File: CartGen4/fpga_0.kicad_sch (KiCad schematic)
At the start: 12 parts, among them U9 LFXP2-8E-5MN132C

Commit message: Assigned all footprints
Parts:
- C19, C20, C21, C22, C23, C24, C25, C30, C31, C32: footprint Capacitor_SMD:C_0402_1005Metric_Pad0.74x0.62mm_HandSolder -> Capacitor_SMD:C_0603_1608Metric_Pad1.08x0.95mm_HandSolder
- R15: footprint (none) -> Resistor_SMD:R_0603_1608Metric_Pad0.98x0.95mm_HandSolder
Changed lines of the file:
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@@
       (effects (font (size 1.27 1.27)) (justify left))
     )
-    (property "Footprint" "Capacitor_SMD:C_0402_1005Metric_Pad0.74x0.62mm_HandSolder" (id 2) (at 205.4352 33.02 0)
+    (property "Footprint" "Capacitor_SMD:C_0603_1608Metric_Pad1.08x0.95mm_HandSolder" (id 2) (at 205.4352 33.02 0)
       (effects (font (size 1.27 1.27)) hide)
     )
@@
       (effects (font (size 1.27 1.27)) (justify left))
     )
-    (property "Footprint" "Capacitor_SMD:C_0402_1005Metric_Pad0.74x0.62mm_HandSolder" (id 2) (at 40.3352 160.02 0)
+    (property "Footprint" "Capacitor_SMD:C_0603_1608Metric_Pad1.08x0.95mm_HandSolder" (id 2) (at 40.3352 160.02 0)
       (effects (font (size 1.27 1.27)) hide)
     )
@@
       (effects (font (size 1.27 1.27)) (justify left))
     )
-    (property "Footprint" "Capacitor_SMD:C_0402_1005Metric_Pad0.74x0.62mm_HandSolder" (id 2) (at 117.8052 40.64 0)
+    (property "Footprint" "Capacitor_SMD:C_0603_1608Metric_Pad1.08x0.95mm_HandSolder" (id 2) (at 117.8052 40.64 0)
       (effects (font (size 1.27 1.27)) hide)
     )
@@
       (effects (font (size 1.27 1.27)) (justify left))
     )
-    (property "Footprint" "" (id 2) (at 75.692 133.35 90)
+    (property "Footprint" "Resistor_SMD:R_0603_1608Metric_Pad0.98x0.95mm_HandSolder" (id 2) (at 75.692 133.35 90)
       (effects (font (size 1.27 1.27)) hide)
     )
@@
       (effects (font (size 1.27 1.27)) (justify left))
     )
-    (property "Footprint" "Capacitor_SMD:C_0402_1005Metric_Pad0.74x0.62mm_HandSolder" (id 2) (at 181.3052 138.43 0)
+    (property "Footprint" "Capacitor_SMD:C_0603_1608Metric_Pad1.08x0.95mm_HandSolder" (id 2) (at 181.3052 138.43 0)
       (effects (font (size 1.27 1.27)) hide)
     )
@@
       (effects (font (size 1.27 1.27)) (justify left))
     )
-    (property "Footprint" "Capacitor_SMD:C_0402_1005Metric_Pad0.74x0.62mm_HandSolder" (id 2) (at 65.7352 137.16 0)
+    (property "Footprint" "Capacitor_SMD:C_0603_1608Metric_Pad1.08x0.95mm_HandSolder" (id 2) (at 65.7352 137.16 0)
       (effects (font (size 1.27 1.27)) hide)
     )
@@
       (effects (font (size 1.27 1.27)) (justify left))
     )
-    (property "Footprint" "Capacitor_SMD:C_0402_1005Metric_Pad0.74x0.62mm_HandSolder" (id 2) (at 53.0352 137.16 0)
+    (property "Footprint" "Capacitor_SMD:C_0603_1608Metric_Pad1.08x0.95mm_HandSolder" (id 2) (at 53.0352 137.16 0)
       (effects (font (size 1.27 1.27)) hide)
     )
@@
       (effects (font (size 1.27 1.27)) (justify left))
     )
-    (property "Footprint" "Capacitor_SMD:C_0402_1005Metric_Pad0.74x0.62mm_HandSolder" (id 2) (at 27.6352 57.15 0)
+    (property "Footprint" "Capacitor_SMD:C_0603_1608Metric_Pad1.08x0.95mm_HandSolder" (id 2) (at 27.6352 57.15 0)
       (effects (font (size 1.27 1.27)) hide)
     )
@@
       (effects (font (size 1.27 1.27)) (justify left))
     )
-    (property "Footprint" "Capacitor_SMD:C_0402_1005Metric_Pad0.74x0.62mm_HandSolder" (id 2) (at 40.3352 137.16 0)
+    (property "Footprint" "Capacitor_SMD:C_0603_1608Metric_Pad1.08x0.95mm_HandSolder" (id 2) (at 40.3352 137.16 0)
       (effects (font (size 1.27 1.27)) hide)
     )
@@
       (effects (font (size 1.27 1.27)) (justify left))
     )
-    (property "Footprint" "Capacitor_SMD:C_0402_1005Metric_Pad0.74x0.62mm_HandSolder" (id 2) (at 53.0352 160.02 0)
+    (property "Footprint" "Capacitor_SMD:C_0603_1608Metric_Pad1.08x0.95mm_HandSolder" (id 2) (at 53.0352 160.02 0)
       (effects (font (size 1.27 1.27)) hide)
     )
@@
       (effects (font (size 1.27 1.27)) (justify left))
     )
-    (property "Footprint" "Capacitor_SMD:C_0402_1005Metric_Pad0.74x0.62mm_HandSolder" (id 2) (at 65.7352 160.02 0)
-      (effects (font (size 1.27 1.27)) hide)
-    )
+    (property "Footprint" "Capacitor_SMD:C_0603_1608Metric_Pad1.08x0.95mm_HandSolder" (id 2) (at 65.7352 160.02 0)
+      (effects (font (size 1.27 1.27)) hide)
+    )

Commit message: Changed most R and C to 0402 size
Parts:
- C19, C20, C21, C22, C23, C24, C25, C30, C31, C32: footprint Capacitor_SMD:C_0603_1608Metric_Pad1.08x0.95mm_HandSolder -> Capacitor_SMD:C_0402_1005Metric_Pad0.74x0.62mm_HandSolder
- R15: footprint Resistor_SMD:R_0603_1608Metric_Pad0.98x0.95mm_HandSolder -> Resistor_SMD:R_0402_1005Metric_Pad0.72x0.64mm_HandSolder
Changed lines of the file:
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@@
       (effects (font (size 1.27 1.27)) (justify left))
     )
-    (property "Footprint" "Capacitor_SMD:C_0603_1608Metric_Pad1.08x0.95mm_HandSolder" (id 2) (at 205.4352 33.02 0)
+    (property "Footprint" "Capacitor_SMD:C_0402_1005Metric_Pad0.74x0.62mm_HandSolder" (id 2) (at 205.4352 33.02 0)
       (effects (font (size 1.27 1.27)) hide)
     )
@@
       (effects (font (size 1.27 1.27)) (justify left))
     )
-    (property "Footprint" "Capacitor_SMD:C_0603_1608Metric_Pad1.08x0.95mm_HandSolder" (id 2) (at 40.3352 160.02 0)
+    (property "Footprint" "Capacitor_SMD:C_0402_1005Metric_Pad0.74x0.62mm_HandSolder" (id 2) (at 40.3352 160.02 0)
       (effects (font (size 1.27 1.27)) hide)
     )
@@
       (effects (font (size 1.27 1.27)) (justify left))
     )
-    (property "Footprint" "Capacitor_SMD:C_0603_1608Metric_Pad1.08x0.95mm_HandSolder" (id 2) (at 117.8052 40.64 0)
+    (property "Footprint" "Capacitor_SMD:C_0402_1005Metric_Pad0.74x0.62mm_HandSolder" (id 2) (at 117.8052 40.64 0)
       (effects (font (size 1.27 1.27)) hide)
     )
@@
       (effects (font (size 1.27 1.27)) (justify left))
     )
-    (property "Footprint" "Resistor_SMD:R_0603_1608Metric_Pad0.98x0.95mm_HandSolder" (id 2) (at 75.692 133.35 90)
+    (property "Footprint" "Resistor_SMD:R_0402_1005Metric_Pad0.72x0.64mm_HandSolder" (id 2) (at 75.692 133.35 90)
       (effects (font (size 1.27 1.27)) hide)
     )
@@
       (effects (font (size 1.27 1.27)) (justify left))
     )
-    (property "Footprint" "Capacitor_SMD:C_0603_1608Metric_Pad1.08x0.95mm_HandSolder" (id 2) (at 181.3052 138.43 0)
+    (property "Footprint" "Capacitor_SMD:C_0402_1005Metric_Pad0.74x0.62mm_HandSolder" (id 2) (at 181.3052 138.43 0)
       (effects (font (size 1.27 1.27)) hide)
     )
@@
       (effects (font (size 1.27 1.27)) (justify left))
     )
-    (property "Footprint" "Capacitor_SMD:C_0603_1608Metric_Pad1.08x0.95mm_HandSolder" (id 2) (at 65.7352 137.16 0)
+    (property "Footprint" "Capacitor_SMD:C_0402_1005Metric_Pad0.74x0.62mm_HandSolder" (id 2) (at 65.7352 137.16 0)
       (effects (font (size 1.27 1.27)) hide)
     )
@@
       (effects (font (size 1.27 1.27)) (justify left))
     )
-    (property "Footprint" "Capacitor_SMD:C_0603_1608Metric_Pad1.08x0.95mm_HandSolder" (id 2) (at 53.0352 137.16 0)
+    (property "Footprint" "Capacitor_SMD:C_0402_1005Metric_Pad0.74x0.62mm_HandSolder" (id 2) (at 53.0352 137.16 0)
       (effects (font (size 1.27 1.27)) hide)
     )
@@
       (effects (font (size 1.27 1.27)) (justify left))
     )
-    (property "Footprint" "Capacitor_SMD:C_0603_1608Metric_Pad1.08x0.95mm_HandSolder" (id 2) (at 27.6352 57.15 0)
+    (property "Footprint" "Capacitor_SMD:C_0402_1005Metric_Pad0.74x0.62mm_HandSolder" (id 2) (at 27.6352 57.15 0)
       (effects (font (size 1.27 1.27)) hide)
     )
@@
       (effects (font (size 1.27 1.27)) (justify left))
     )
-    (property "Footprint" "Capacitor_SMD:C_0603_1608Metric_Pad1.08x0.95mm_HandSolder" (id 2) (at 40.3352 137.16 0)
+    (property "Footprint" "Capacitor_SMD:C_0402_1005Metric_Pad0.74x0.62mm_HandSolder" (id 2) (at 40.3352 137.16 0)
       (effects (font (size 1.27 1.27)) hide)
     )
@@
       (effects (font (size 1.27 1.27)) (justify left))
     )
-    (property "Footprint" "Capacitor_SMD:C_0603_1608Metric_Pad1.08x0.95mm_HandSolder" (id 2) (at 53.0352 160.02 0)
+    (property "Footprint" "Capacitor_SMD:C_0402_1005Metric_Pad0.74x0.62mm_HandSolder" (id 2) (at 53.0352 160.02 0)
       (effects (font (size 1.27 1.27)) hide)
     )
@@
       (effects (font (size 1.27 1.27)) (justify left))
     )
-    (property "Footprint" "Capacitor_SMD:C_0603_1608Metric_Pad1.08x0.95mm_HandSolder" (id 2) (at 65.7352 160.02 0)
-      (effects (font (size 1.27 1.27)) hide)
-    )
+    (property "Footprint" "Capacitor_SMD:C_0402_1005Metric_Pad0.74x0.62mm_HandSolder" (id 2) (at 65.7352 160.02 0)
+      (effects (font (size 1.27 1.27)) hide)
+    )

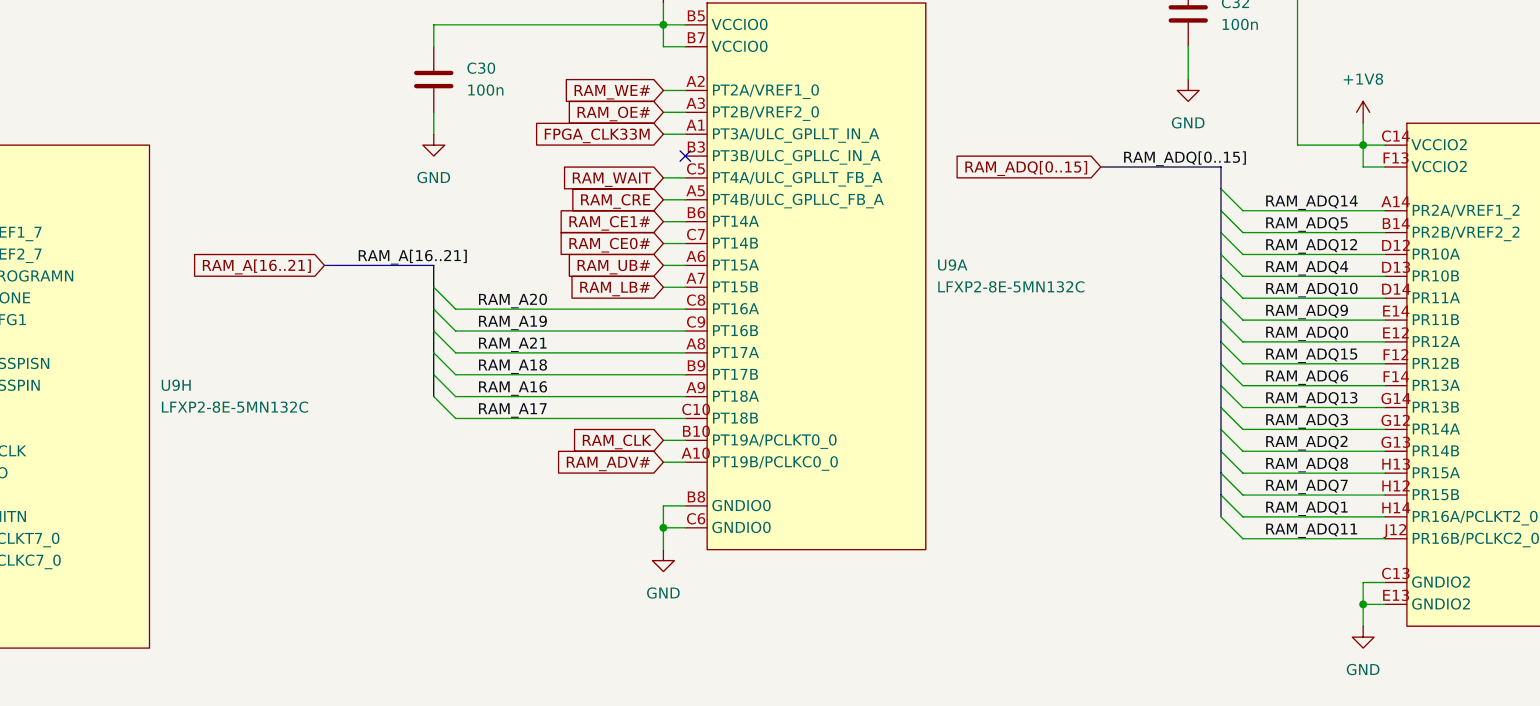
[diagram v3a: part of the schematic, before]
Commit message: Started routing RAM
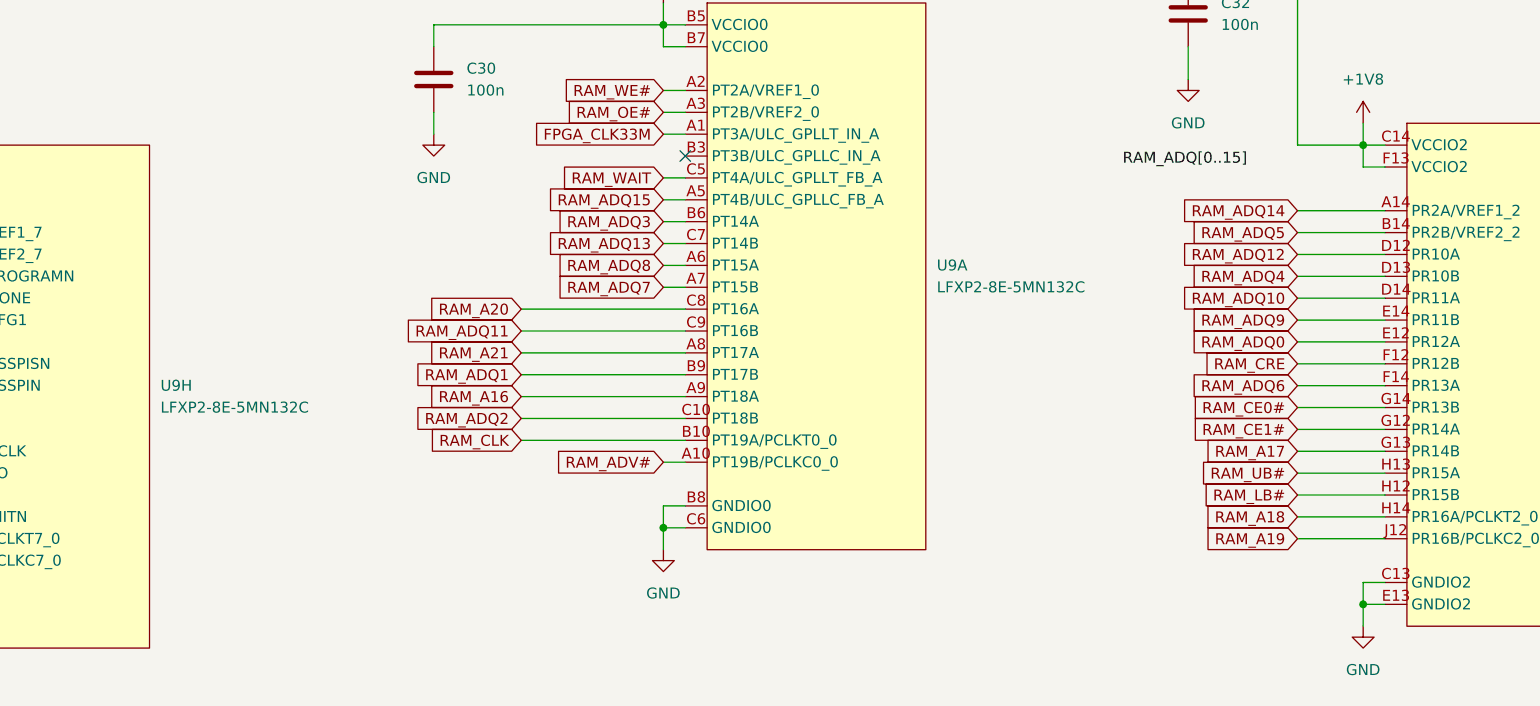
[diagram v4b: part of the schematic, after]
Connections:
- net RAM_A17: now also U9.G13 (PR14B); no longer U9.C10 (PT18B)
- net RAM_A18: now also U9.H14 (PR16A/PCLKT2_0); no longer U9.B9 (PT17B)
- net RAM_A19: now also U9.J12 (PR16B/PCLKC2_0); no longer U9.C9 (PT16B)
- net RAM_ADQ1: now also U9.B9 (PT17B); no longer U9.H14 (PR16A/PCLKT2_0)
- net RAM_ADQ11: now also U9.C9 (PT16B); no longer U9.J12 (PR16B/PCLKC2_0)
- net RAM_ADQ13: now also U9.C7 (PT14B); no longer U9.G14 (PR13B)
- net RAM_ADQ15: now also U9.A5 (PT4B/ULC_GPLLC_FB_A); no longer U9.F12 (PR12B)
- net RAM_ADQ2: now also U9.C10 (PT18B); no longer U9.G13 (PR14B)
- net RAM_ADQ3: now also U9.B6 (PT14A); no longer U9.G12 (PR14A)
- net RAM_ADQ7: now also U9.A7 (PT15B); no longer U9.H12 (PR15B)
- net RAM_ADQ8: now also U9.A6 (PT15A); no longer U9.H13 (PR15A)
- net RAM_CE0#: now also U9.G14 (PR13B); no longer U9.C7 (PT14B)
- net RAM_CE1#: now also U9.G12 (PR14A); no longer U9.B6 (PT14A)
- net RAM_CRE: now also U9.F12 (PR12B); no longer U9.A5 (PT4B/ULC_GPLLC_FB_A)
- net RAM_LB#: now also U9.H12 (PR15B); no longer U9.A7 (PT15B)
- net RAM_UB#: now also U9.H13 (PR15A); no longer U9.A6 (PT15A)

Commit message: Started routing more ram, but I'd better sleep...
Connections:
- net RAM_ADQ12: now also U9.F14 (PR13A); no longer U9.D12 (PR10A)
- net RAM_ADQ6: now also U9.D12 (PR10A); no longer U9.F14 (PR13A)
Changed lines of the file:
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@@
-    )
-  )
-  (global_label "RAM_ADQ12" (shape input) (at 217.1625 57.15 180) (fields_autoplaced)
-    (effects (font (size 1.27 1.27)) (justify right))
-    (property "Intersheet References" "${INTERSHEET_REFS}" (id 0) (at 203.8637 57.0706 0)
-      (effects (font (size 1.27 1.27)) (justify right) hide)
     )
   )
@@
     )
   )
+  (global_label "RAM_ADQ6" (shape input) (at 217.17 57.15 180) (fields_autoplaced)
+    (effects (font (size 1.27 1.27)) (justify right))
+    (property "Intersheet References" "${INTERSHEET_REFS}" (id 0) (at 205.0807 57.0706 0)
+      (effects (font (size 1.27 1.27)) (justify right) hide)
+    )
+  )
   (global_label "PS_PGOOD" (shape input) (at 53.34 87.63 180) (fields_autoplaced)
     (effects (font (size 1.27 1.27)) (justify right))
@@
     (effects (font (size 1.27 1.27)) (justify right))
     (property "Intersheet References" "${INTERSHEET_REFS}" (id 0) (at 205.0732 59.6106 0)
+      (effects (font (size 1.27 1.27)) (justify right) hide)
+    )
+  )
+  (global_label "RAM_ADQ12" (shape input) (at 217.1625 72.39 180) (fields_autoplaced)
+    (effects (font (size 1.27 1.27)) (justify right))
+    (property "Intersheet References" "${INTERSHEET_REFS}" (id 0) (at 203.8637 72.3106 0)
       (effects (font (size 1.27 1.27)) (justify right) hide)
     )
@@
       (effects (font (size 1.27 1.27)) (justify right) hide)
     )
-  )
-  (global_label "RAM_ADQ6" (shape input) (at 217.1625 72.39 180) (fields_autoplaced)
-    (effects (font (size 1.27 1.27)) (justify right))
-    (property "Intersheet References" "${INTERSHEET_REFS}" (id 0) (at 205.0732 72.3106 0)
-      (effects (font (size 1.27 1.27)) (justify right) hide)
-    )

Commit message: More RAM wire changes (i wanna cry)
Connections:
- net RAM_A16: now also U9.E12 (PR12A); no longer U9.A9 (PT18A)
- net RAM_A19: now also U9.H13 (PR15A); no longer U9.J12 (PR16B/PCLKC2_0)
- net RAM_A20: now also U9.D13 (PR10B); no longer U9.C8 (PT16A)
- net RAM_A21: now also U9.E14 (PR11B); no longer U9.A8 (PT17A)
- net RAM_ADQ0: now also U9.A6 (PT15A); no longer U9.E12 (PR12A)
- net RAM_ADQ1: now also U9.A2 (PT2A/VREF1_0); no longer U9.B9 (PT17B)
- net RAM_ADQ10: now also U9.A8 (PT17A); no longer U9.D14 (PR11A)
- net RAM_ADQ11: now also U9.A3 (PT2B/VREF2_0); no longer U9.C9 (PT16B)
- net RAM_ADQ13: now also U9.C10 (PT18B); no longer U9.C7 (PT14B)
- net RAM_ADQ14: now also U9.A9 (PT18A); no longer U9.A14 (PR2A/VREF1_2)
- net RAM_ADQ15: now also U9.A14 (PR2A/VREF1_2); no longer U9.A5 (PT4B/ULC_GPLLC_FB_A)
- net RAM_ADQ2: now also U9.B6 (PT14A); no longer U9.C10 (PT18B)
- net RAM_ADQ3: now also U9.A7 (PT15B); no longer U9.B6 (PT14A)
- net RAM_ADQ4: now also U9.B14 (PR2B/VREF2_2); no longer U9.D13 (PR10B)
- net RAM_ADQ5: now also U9.B9 (PT17B); no longer U9.B14 (PR2B/VREF2_2)
- net RAM_ADQ6: now also U9.A10 (PT19B/PCLKC0_0); no longer U9.D12 (PR10A)
- net RAM_ADQ7: now also U9.D14 (PR11A); no longer U9.A7 (PT15B)
- net RAM_ADQ8: now also U9.A5 (PT4B/ULC_GPLLC_FB_A); no longer U9.A6 (PT15A)
- net RAM_ADQ9: now also U9.C8 (PT16A); no longer U9.E14 (PR11B)
- net RAM_ADV#: now also U9.C7 (PT14B); no longer U9.A10 (PT19B/PCLKC0_0)
- net RAM_OE#: now also U9.C9 (PT16B); no longer U9.A3 (PT2B/VREF2_0)
- net RAM_UB#: now also U9.J12 (PR16B/PCLKC2_0); no longer U9.H13 (PR15A)
- net RAM_WE#: now also U9.D12 (PR10A); no longer U9.A2 (PT2A/VREF1_0)

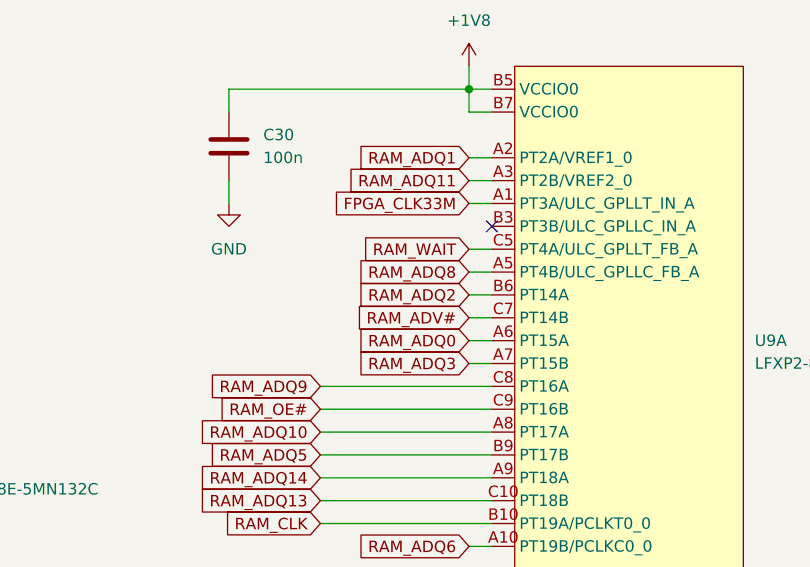
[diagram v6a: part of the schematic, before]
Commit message: Wired all RAM signal wires (finally...)
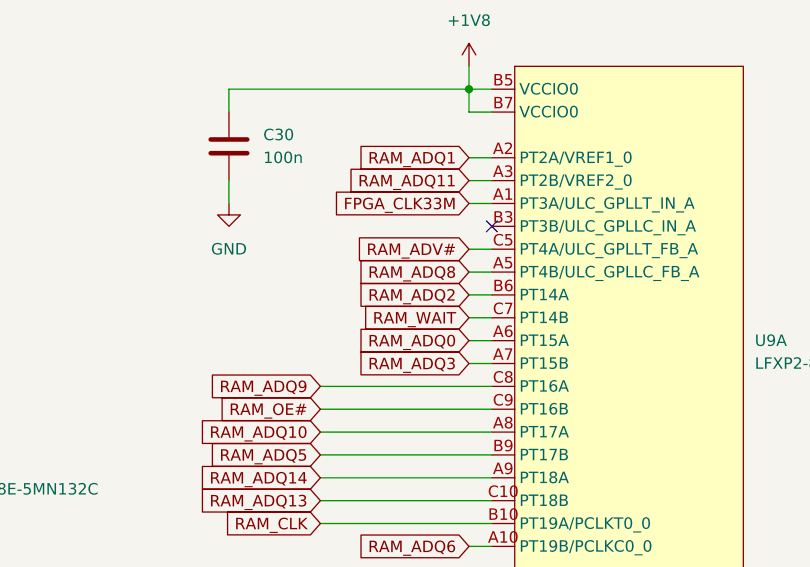
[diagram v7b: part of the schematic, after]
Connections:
- net RAM_ADV#: now also U9.C5 (PT4A/ULC_GPLLT_FB_A); no longer U9.C7 (PT14B)
- net RAM_WAIT: now also U9.C7 (PT14B); no longer U9.C5 (PT4A/ULC_GPLLT_FB_A)
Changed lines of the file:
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@@
-    )
-  )
-  (global_label "RAM_OE#" (shape input) (at 127 66.04 180) (fields_autoplaced)
-    (effects (font (size 1.27 1.27)) (justify right))
-    (property "Intersheet References" "${INTERSHEET_REFS}" (id 0) (at 116.0598 65.9606 0)
-      (effects (font (size 1.27 1.27)) (justify right) hide)
     )
   )
@@
     (effects (font (size 1.27 1.27)) (justify right))
     (property "Intersheet References" "${INTERSHEET_REFS}" (id 0) (at 206.4717 79.9306 0)
+      (effects (font (size 1.27 1.27)) (justify right) hide)
+    )
+  )
+  (global_label "RAM_OE#" (shape input) (at 127 66.04 180) (fields_autoplaced)
+    (effects (font (size 1.27 1.27)) (justify right))
+    (property "Intersheet References" "${INTERSHEET_REFS}" (id 0) (at 116.0598 65.9606 0)
       (effects (font (size 1.27 1.27)) (justify right) hide)
     )
@@
     (effects (font (size 1.27 1.27)) (justify right))
     (property "Intersheet References" "${INTERSHEET_REFS}" (id 0) (at 206.4717 59.6106 0)
-      (effects (font (size 1.27 1.27)) (justify right) hide)
-    )
-  )
-  (global_label "RAM_ADV#" (shape input) (at 143.51 55.88 180) (fields_autoplaced)
-    (effects (font (size 1.27 1.27)) (justify right))
-    (property "Intersheet References" "${INTERSHEET_REFS}" (id 0) (at 131.6021 55.8006 0)
       (effects (font (size 1.27 1.27)) (justify right) hide)
     )
@@
     (effects (font (size 1.27 1.27)) (justify right))
     (property "Intersheet References" "${INTERSHEET_REFS}" (id 0) (at 34.9612 77.5494 0)
+      (effects (font (size 1.27 1.27)) (justify right) hide)
+    )
+  )
+  (global_label "RAM_WAIT" (shape input) (at 143.51 55.88 180) (fields_autoplaced)
+    (effects (font (size 1.27 1.27)) (justify right))
+    (property "Intersheet References" "${INTERSHEET_REFS}" (id 0) (at 132.2069 55.8006 0)
       (effects (font (size 1.27 1.27)) (justify right) hide)
     )
@@
     )
   )
-  (global_label "RAM_WAIT" (shape input) (at 143.51 48.26 180) (fields_autoplaced)
-    (effects (font (size 1.27 1.27)) (justify right))
-    (property "Intersheet References" "${INTERSHEET_REFS}" (id 0) (at 132.2069 48.1806 0)
-      (effects (font (size 1.27 1.27)) (justify right) hide)
-    )
-  )
   (global_label "FPGA_JTAG_TDO" (shape input) (at 209.55 140.97 180) (fields_autoplaced)
     (effects (font (size 1.27 1.27)) (justify right))
@@
       (effects (font (size 1.27 1.27)) (justify right) hide)
     )
+  )
+  (global_label "RAM_ADV#" (shape input) (at 143.51 48.26 180) (fields_autoplaced)
+    (effects (font (size 1.27 1.27)) (justify right))
+    (property "Intersheet References" "${INTERSHEET_REFS}" (id 0) (at 131.6021 48.1806 0)
+      (effects (font (size 1.27 1.27)) (justify right) hide)
+    )
